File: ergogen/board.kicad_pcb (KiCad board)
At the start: 2 copper layers, 155.6 x 110.2 mm, 50 parts

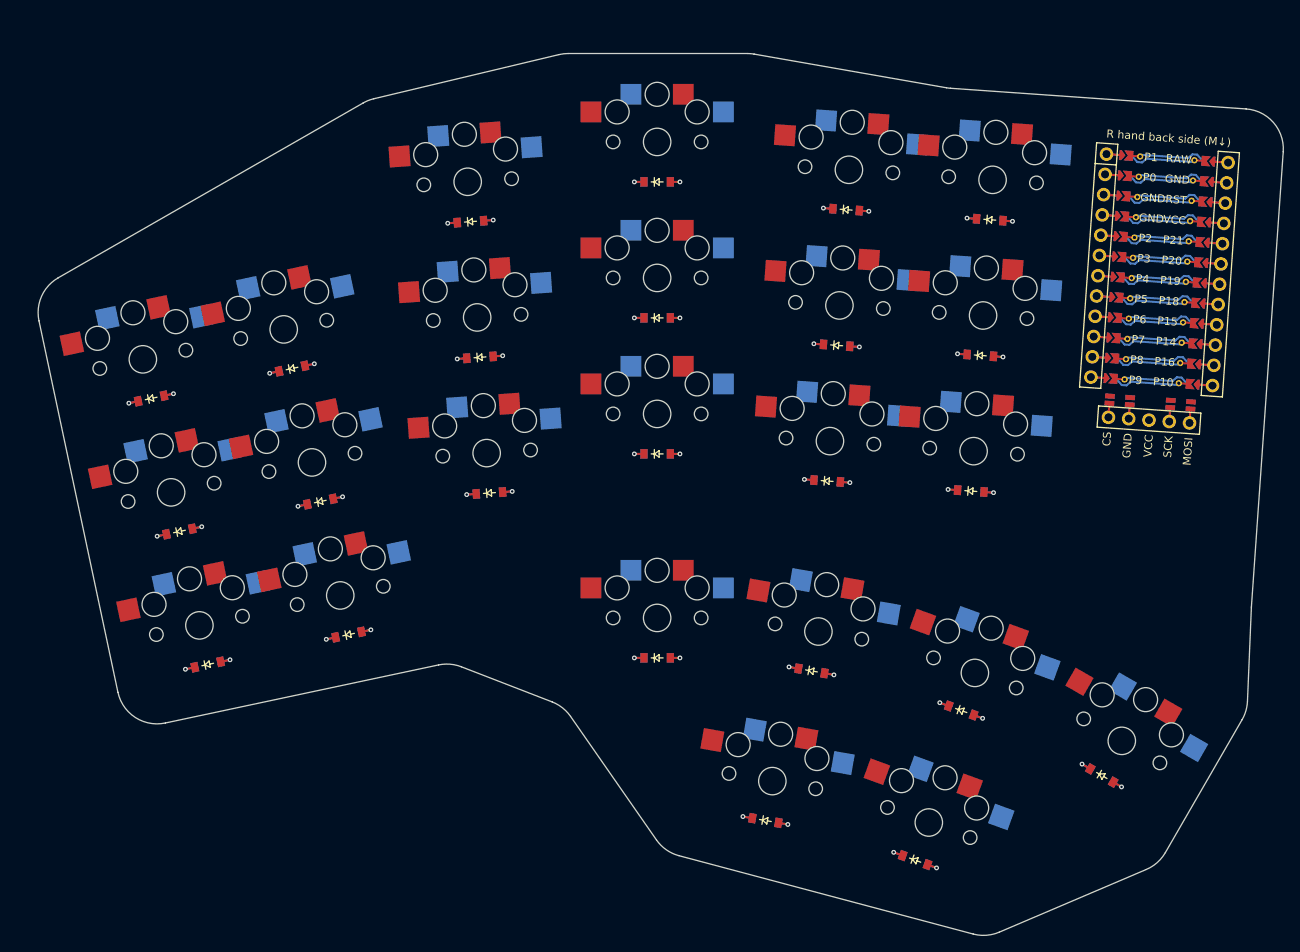
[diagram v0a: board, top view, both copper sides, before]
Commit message: picked pins for the matrix
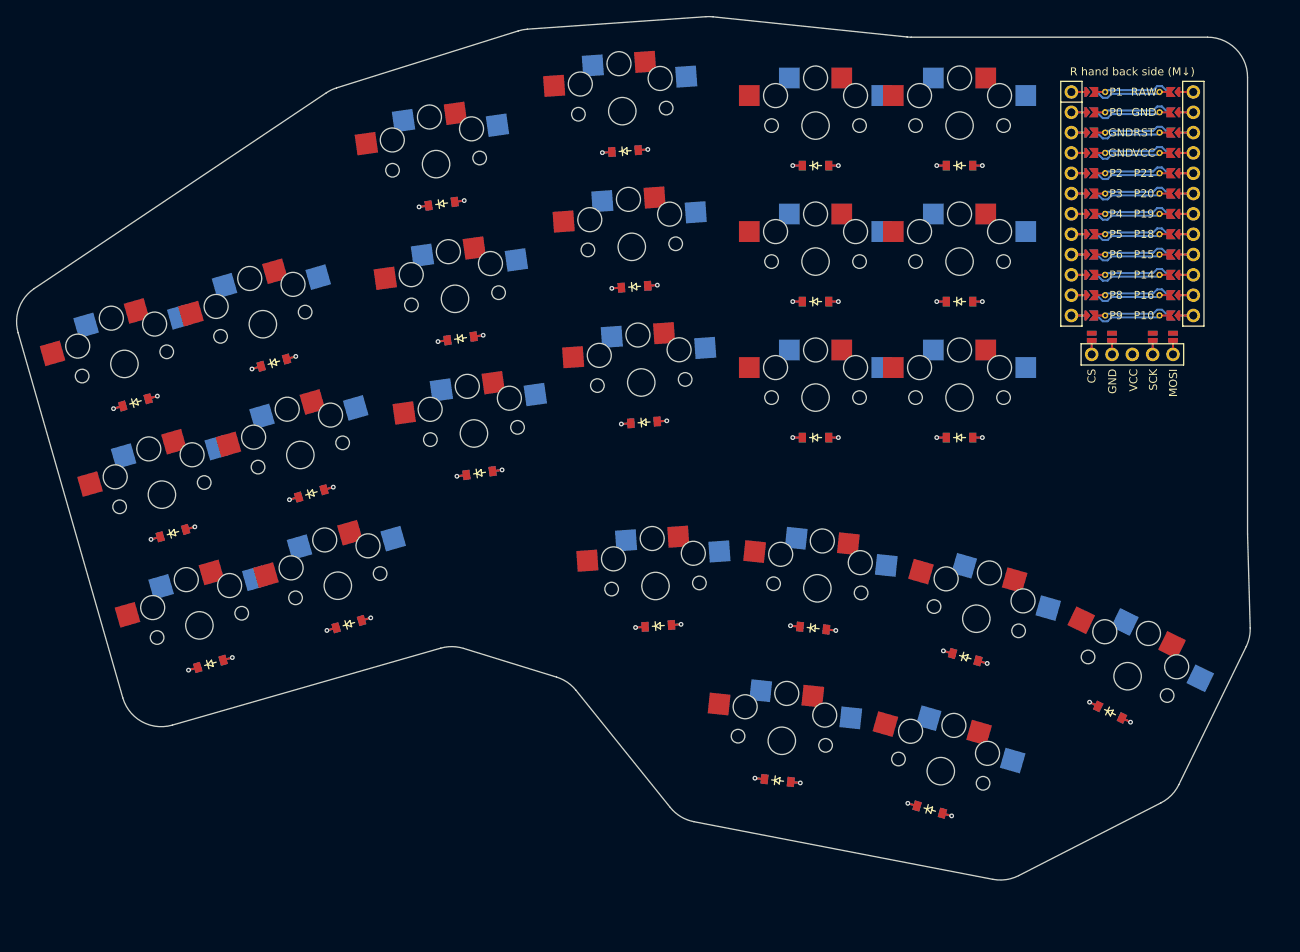
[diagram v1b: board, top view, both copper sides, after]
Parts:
- moved MCU1 8.97 mm to (266.6, 96.0), turned to 0 degrees
- moved DISP1 8.87 mm to (266.6, 99.4), turned to 0 degrees
- moved S22 8.11 mm to (266.0, 156.4), turned to -26 degrees
- moved D22 7.98 mm to (263.8, 160.8), turned to -26 degrees
- moved S18 7.94 mm to (245.0, 87.5), turned to 0 degrees
- moved D18 7.75 mm to (245.0, 92.5), turned to 0 degrees
- moved S17 7.35 mm to (245.0, 104.5), turned to 0 degrees
- moved D17 7.21 mm to (245.0, 109.5), turned to 0 degrees
- moved S16 6.92 mm to (245.0, 121.5), turned to 0 degrees
- moved S15 6.92 mm to (227.0, 87.5), turned to 0 degrees
- moved D16 6.83 mm to (245.0, 126.5), turned to 0 degrees
- moved S21 6.78 mm to (247.1, 149.2), turned to -16 degrees
- moved D15 6.71 mm to (227.0, 92.5), turned to 0 degrees
- moved D21 6.69 mm to (245.7, 154.0), turned to -16 degrees
- moved S24 6.59 mm to (242.7, 168.2), turned to -16 degrees
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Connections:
- net home_top renamed tt_home_tt_top
- net inner_bot renamed tb_inner_tb_bot
- net outer_bot renamed tb_outer_tb_bot
- D1 pad 1: P6 -> P18
- D10 pad 1: P6 -> P18
- D11 pad 1: P7 -> P19
- D12 pad 1: P8 -> P20
- D13 pad 1: P6 -> P18
- D14 pad 1: P7 -> P19
- D15 pad 1: P8 -> P20
- D16 pad 1: P6 -> P18
- D17 pad 1: P7 -> P19
- D18 pad 1: P8 -> P20
- D19 pad 1: P9 -> P21
- D19 pad 2: outer_top -> tt_outer_tt_top
- D2 pad 1: P7 -> P19
- D20 pad 1: P9 -> P21
- D20 pad 2: middle_top -> tt_middle_tt_top
- D21 pad 1: P9 -> P21
- D22 pad 1: P9 -> P21
- D22 pad 2: inner_top -> tt_inner_tt_top
- D23 pad 1: P9 -> P21
- D24 pad 1: P9 -> P21
- D3 pad 1: P8 -> P20
- D4 pad 1: P6 -> P18
- D5 pad 1: P7 -> P19
- D6 pad 1: P8 -> P20
- D7 pad 1: P6 -> P18
- D8 pad 1: P7 -> P19
- D9 pad 1: P8 -> P20
- S1 pad 1: P0 -> P8
- S10 pad 1: P3 -> P14
- S11 pad 1: P3 -> P14
- S12 pad 1: P3 -> P14
- S13 pad 1: P4 -> P15
- S14 pad 1: P4 -> P15
- S15 pad 1: P4 -> P15
- S16 pad 1: P5 -> P16
- S17 pad 1: P5 -> P16
- S18 pad 1: P5 -> P16
- S19 pad 1: P0 -> P9
- S19 pad 2: outer_top -> tt_outer_tt_top
- S2 pad 1: P0 -> P8
- S20 pad 1: P1 -> P10
- S20 pad 2: middle_top -> tt_middle_tt_top
- S21 pad 1: P2 -> P15
- S22 pad 1: P3 -> P16
- S22 pad 2: inner_top -> tt_inner_tt_top
- S23 pad 1: P4 -> P8
- S24 pad 1: P5 -> P14
- S3 pad 1: P0 -> P8
- S4 pad 1: P1 -> P9
- S5 pad 1: P1 -> P9
- S6 pad 1: P1 -> P9
- S7 pad 1: P2 -> P10
- S8 pad 1: P2 -> P10
- S9 pad 1: P2 -> P10
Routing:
- net P9: track 14.4 -> 0.00 mm, vias 6 -> 0
- net P8: track 14.4 -> 0.00 mm, vias 6 -> 0
- net P7: track 14.4 -> 0.00 mm, vias 6 -> 0
- net P6: track 14.4 -> 0.00 mm, vias 6 -> 0
- net P20: track 0.00 -> 14.4 mm, vias 0 -> 6
- net P19: track 0.00 -> 14.4 mm, vias 0 -> 6
- net P18: track 0.00 -> 14.4 mm, vias 0 -> 6
- net P21: track 0.00 -> 14.4 mm, vias 0 -> 6
- net outer_top: track 4.80 -> 2.40 mm, vias 2 -> 1
- net middle_top: track 4.80 -> 2.40 mm, vias 2 -> 1
- net tt_middle_tt_top: track 0.00 -> 2.40 mm, vias 0 -> 1
- net tt_inner_tt_top: track 0.00 -> 2.40 mm, vias 0 -> 1
- net inner_top: track 4.80 -> 2.40 mm, vias 2 -> 1
- net tt_outer_tt_top: track 0.00 -> 2.40 mm, vias 0 -> 1
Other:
- board size 155.6 x 110.2 mm -> 154.2 x 107.9 mm

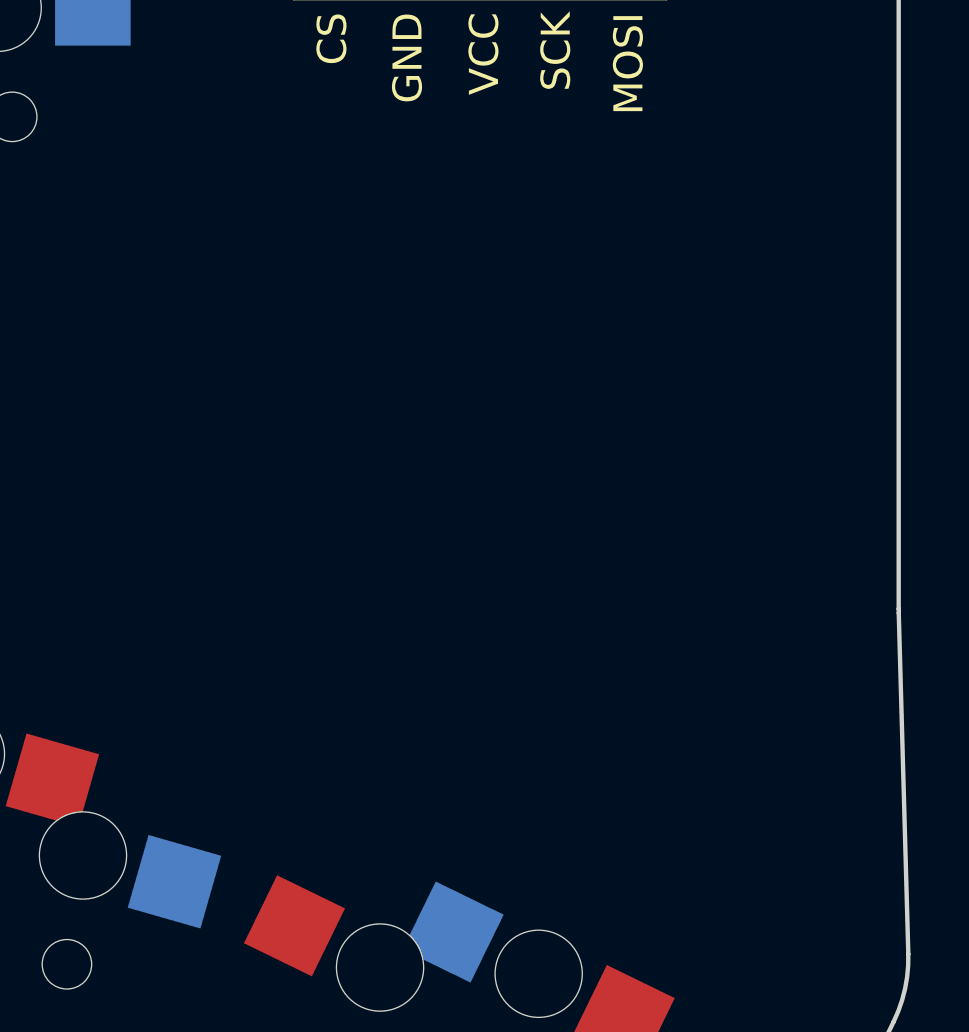
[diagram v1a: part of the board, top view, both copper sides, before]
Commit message: adding switches and battery connector
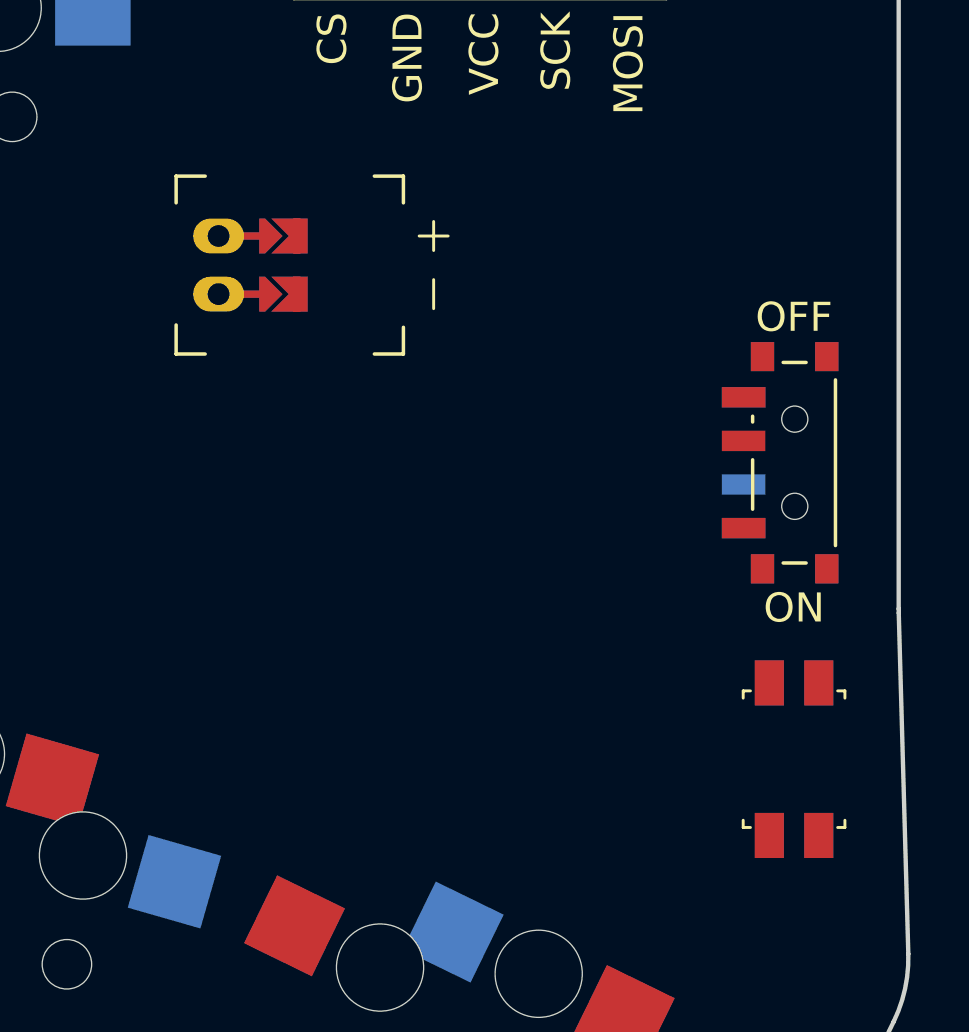
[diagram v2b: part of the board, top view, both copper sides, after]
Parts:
- added JST1: , ceoloide:battery_connector_jst_ph_2, F.Cu at (257.6, 126.6)
- added PWR1: , ceoloide:power_switch_smd_side, F.Cu at (277.4, 133.4)
- added RST1: , ceoloide:reset_switch_smd_side, F.Cu at (277.4, 143.6)
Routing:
- net JST1_2: track 0.00 -> 3.60 mm
- net JST1_1: track 0.00 -> 3.60 mm

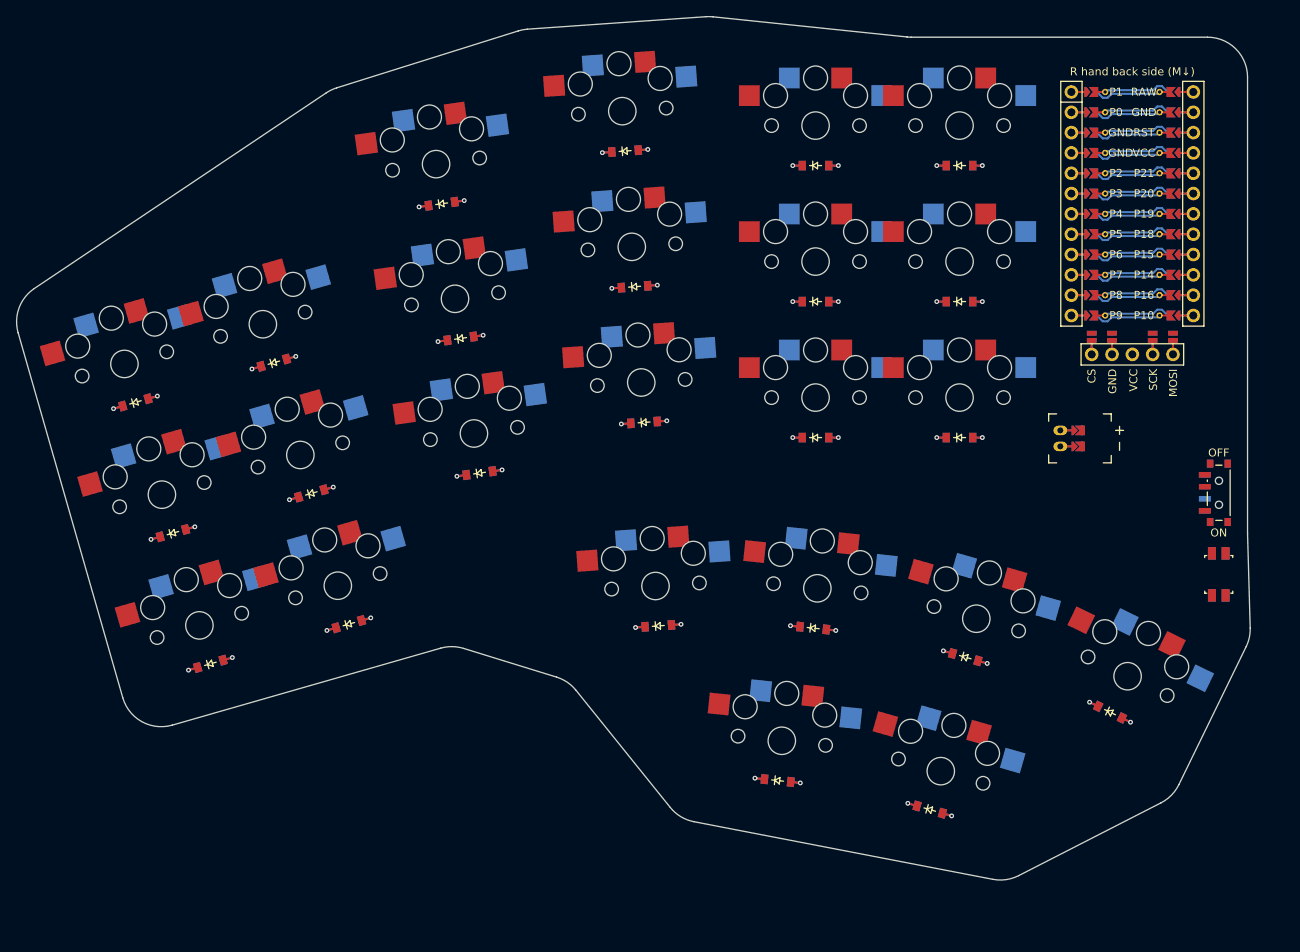
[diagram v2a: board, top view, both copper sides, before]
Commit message: mounting holes
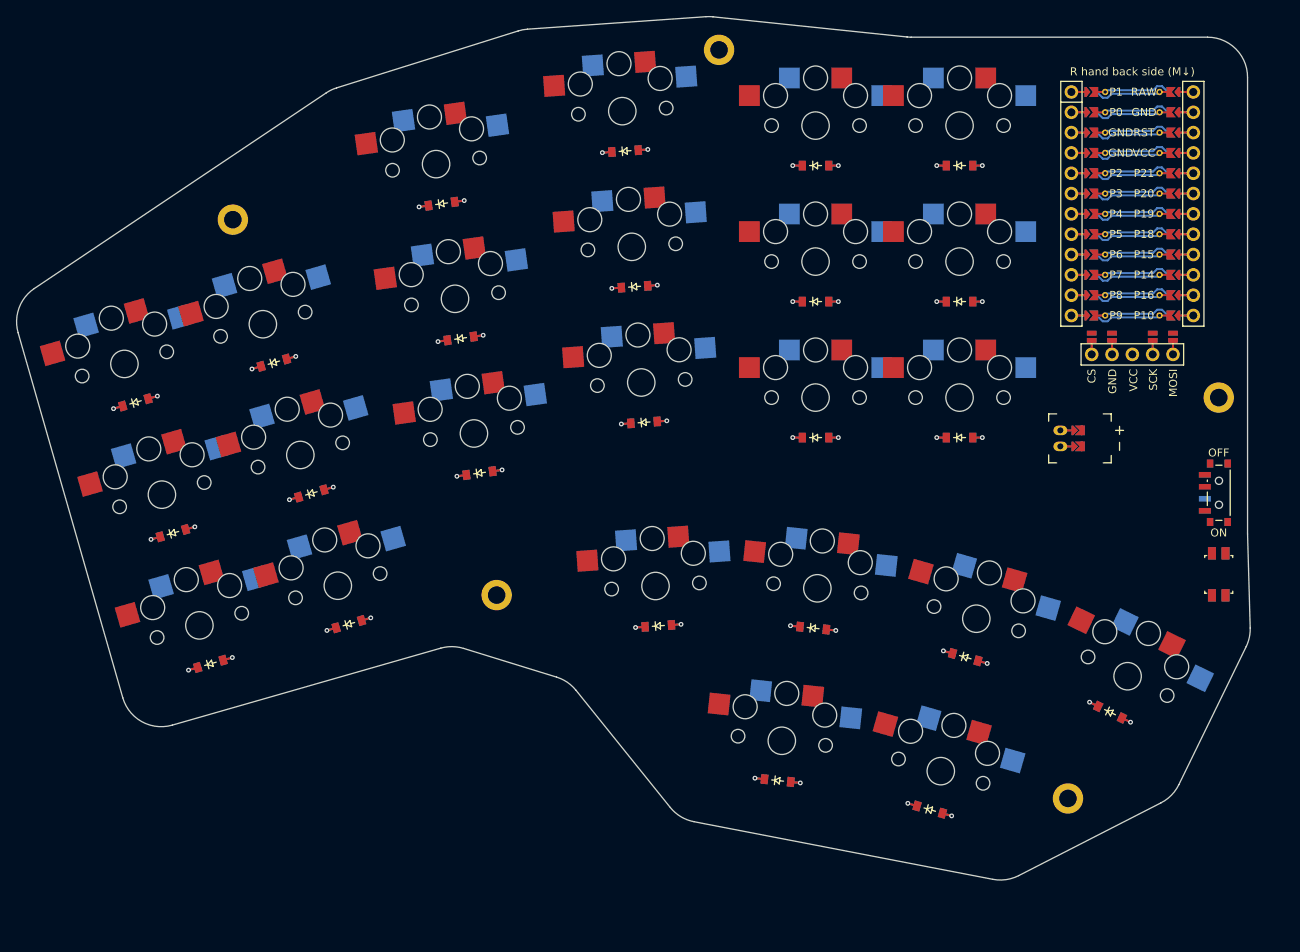
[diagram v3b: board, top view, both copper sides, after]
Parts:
- added H1: , ceoloide:mounting_hole_plated, F.Cu at (154.2, 99.3)
- added H2: , ceoloide:mounting_hole_plated, F.Cu at (187.2, 146.2)
- added H3: , ceoloide:mounting_hole_plated, F.Cu at (215.0, 78.1)
- added H4: , ceoloide:mounting_hole_plated, F.Cu at (258.6, 171.6)
- added H5: , ceoloide:mounting_hole_plated, F.Cu at (277.4, 121.5)
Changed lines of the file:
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@@
     (fp_line (start 2.35 1.5) (end 2.35 1.75) (stroke (width 0.1) (type solid)) (layer "B.SilkS"))
+  )
+  (footprint "ceoloide:mounting_hole_plated"
+    (layer "F.Cu")
+    (at 154.18237249999999 99.28247090000002 16)
+    (property "Reference" "H1"
+      (at 0 3 16)
+      (layer "F.SilkS")
+      hide
+      (effects (font (size 1 1) (thickness 0.15)))
+    )
+    (pad "" thru_hole circle (at 0 0 16) (size 3.8000000000000003 3.8000000000000003) (drill 2.2) (layers "*.Cu" "*.Mask"))
+    (fp_circle (center 0 0) (end -2.1500000000000004 0) (layer "F.CrtYd") (stroke (width 0.05) (type solid)) (fill none))
+    (fp_circle (center 0 0) (end -2.1500000000000004 0) (layer "B.CrtYd") (stroke (width 0.05) (type solid)) (fill none))
+  )
+  (footprint "ceoloide:mounting_hole_plated"
+    (layer "F.Cu")
+    (at 187.1564264 146.2130702 8)
+    (property "Reference" "H2"
+      (at 0 3 8)
+      (layer "F.SilkS")
+      hide
+      (effects (font (size 1 1) (thickness 0.15)))
+    )
+    (pad "" thru_hole circle (at 0 0 8) (size 3.8000000000000003 3.8000000000000003) (drill 2.2) (layers "*.Cu" "*.Mask"))
+    (fp_circle (center 0 0) (end -2.1500000000000004 0) (layer "F.CrtYd") (stroke (width 0.05) (type solid)) (fill none))
+    (fp_circle (center 0 0) (end -2.1500000000000004 0) (layer "B.CrtYd") (stroke (width 0.05) (type solid)) (fill none))
+  )
+  (footprint "ceoloide:mounting_hole_plated"
+    (layer "F.Cu")
+    (at 214.95713959999998 78.05900630000002 4)
+    (property "Reference" "H3"
+      (at 0 3 4)
+      (layer "F.SilkS")
+      hide
+      (effects (font (size 1 1) (thickness 0.15)))
+    )
+    (pad "" thru_hole circle (at 0 0 4) (size 3.8000000000000003 3.8000000000000003) (drill 2.2) (layers "*.Cu" "*.Mask"))
+    (fp_circle (center 0 0) (end -2.1500000000000004 0) (layer "F.CrtYd") (stroke (width 0.05) (type solid)) (fill none))
+    (fp_circle (center 0 0) (end -2.1500000000000004 0) (layer "B.CrtYd") (stroke (width 0.05) (type solid)) (fill none))
+  )
+  (footprint "ceoloide:mounting_hole_plated"
+    (layer "F.Cu")
+    (at 258.57216999999997 171.6344766 -26)
+    (property "Reference" "H4"
+      (at 0 3 -26)
+      (layer "F.SilkS")
+      hide
+      (effects (font (size 1 1) (thickness 0.15)))
+    )
+    (pad "" thru_hole circle (at 0 0 -26) (size 3.8000000000000003 3.8000000000000003) (drill 2.2) (layers "*.Cu" "*.Mask"))
+    (fp_circle (center 0 0) (end -2.1500000000000004 0) (layer "F.CrtYd") (stroke (width 0.05) (type solid)) (fill none))
+    (fp_circle (center 0 0) (end -2.1500000000000004 0) (layer "B.CrtYd") (stroke (width 0.05) (type solid)) (fill none))
+  )
+  (footprint "ceoloide:mounting_hole_plated"
+    (layer "F.Cu")
+    (at 277.4184523 121.52352920000001 0)
+    (property "Reference" "H5"
+      (at 0 3 0)
+      (layer "F.SilkS")
+      hide
+      (effects (font (size 1 1) (thickness 0.15)))
+    )
+    (pad "" thru_hole circle (at 0 0 0) (size 3.8000000000000003 3.8000000000000003) (drill 2.2) (layers "*.Cu" "*.Mask"))
+    (fp_circle (center 0 0) (end -2.1500000000000004 0) (layer "F.CrtYd") (stroke (width 0.05) (type solid)) (fill none))
+    (fp_circle (center 0 0) (end -2.1500000000000004 0) (layer "B.CrtYd") (stroke (width 0.05) (type solid)) (fill none))
   )
   (gr_line (start 140.42084418410485 159.04059049428741) (end 127.34022196451548 113.42303919096764) (angle 90) (layer Edge.Cuts) (width 0.15))

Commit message: connected display pins
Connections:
- MCU1 pad 115: P7 -> CS
- MCU1 pad 116: P6 -> SCK
- MCU1 pad 117: P5 -> MOSI
